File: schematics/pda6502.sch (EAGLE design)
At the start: 26 parts, among them IC1 74HC00D, IC2 74HC138D, IC3 DS1813-SMD, U1 W65C02S, U2 W65C22S, U3 28C256, U4 UM61256AK-12

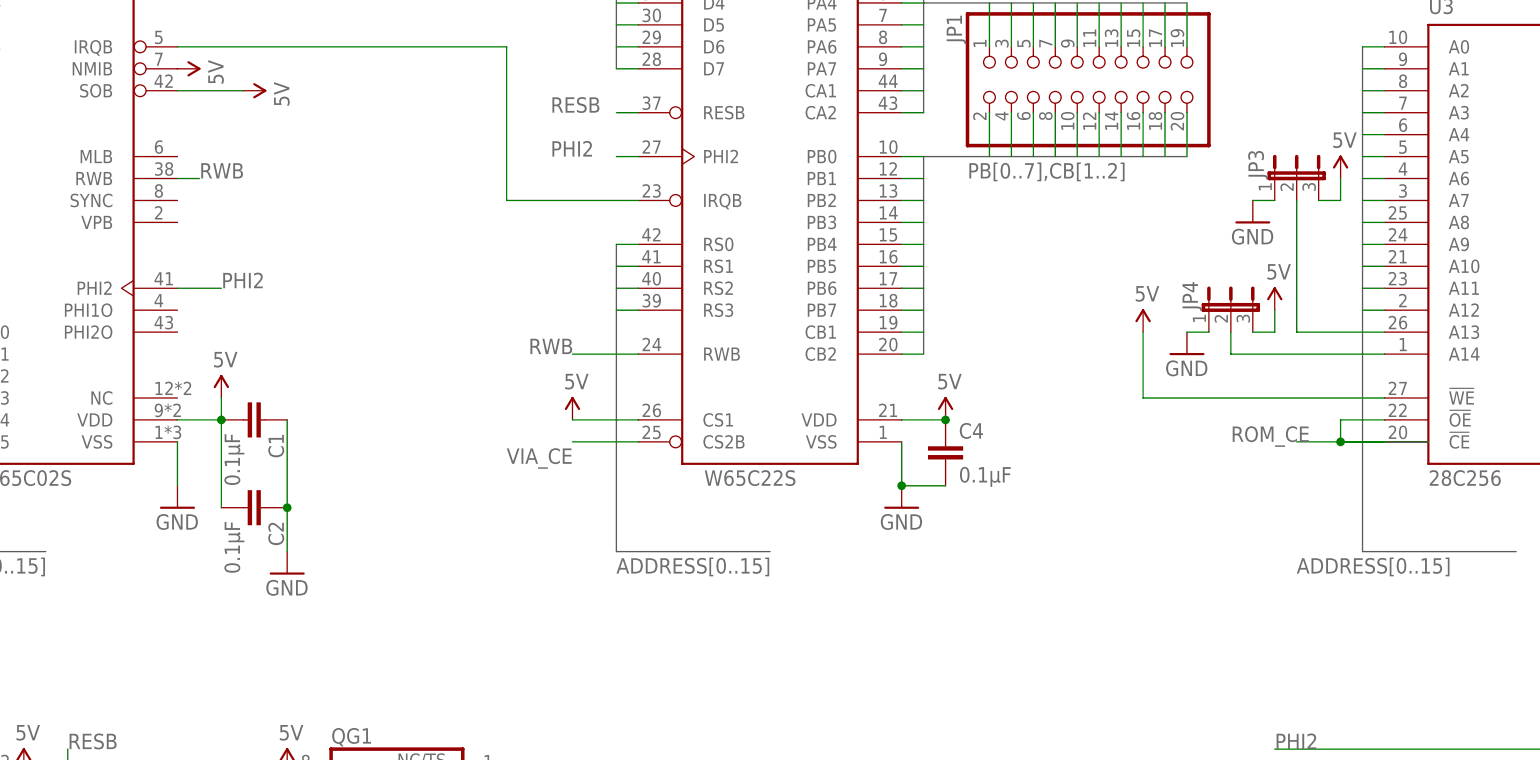
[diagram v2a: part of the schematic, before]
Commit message: schematics: README updates, schematic layout tweaks.
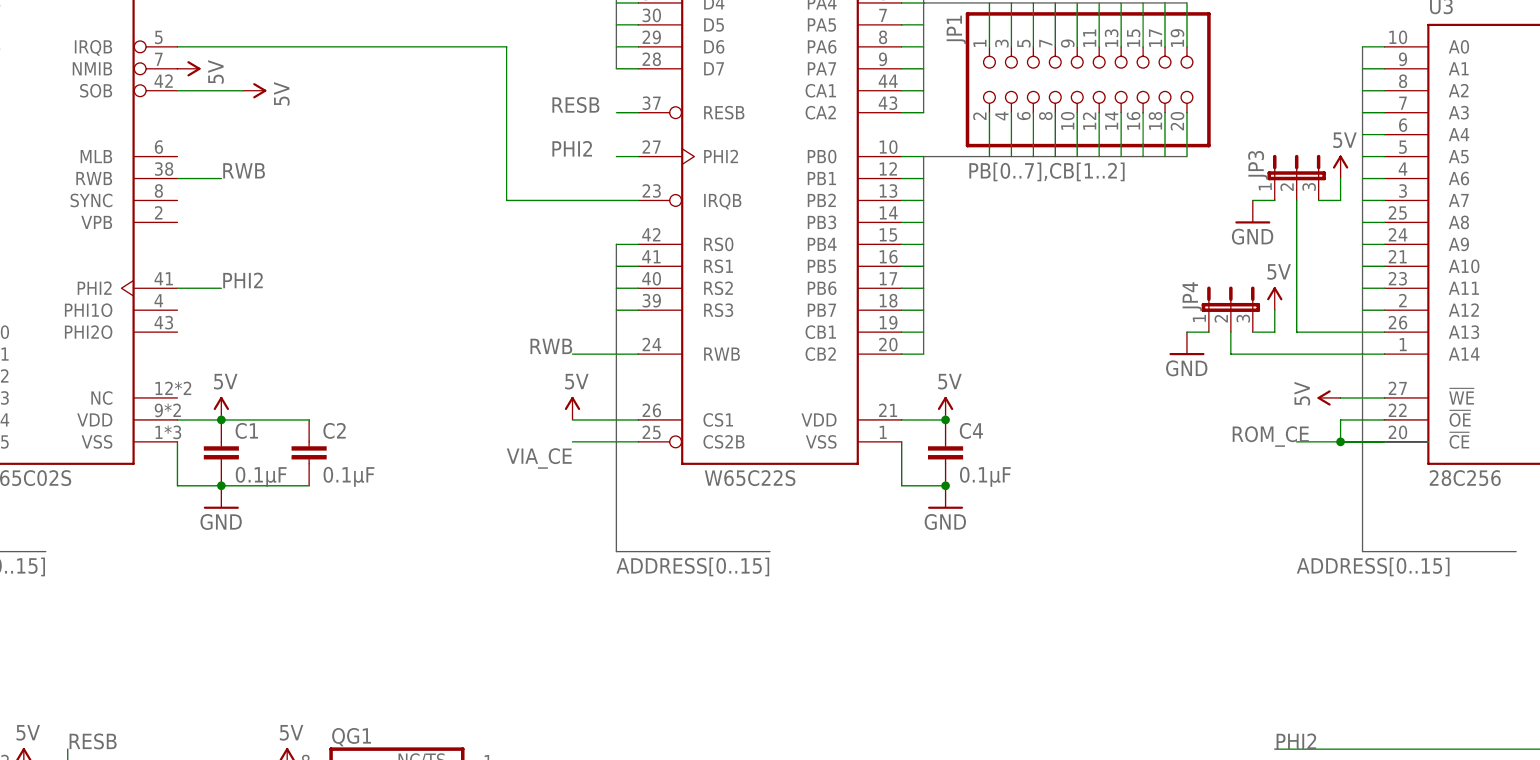
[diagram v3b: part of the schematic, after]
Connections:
- net 5V: now also C1.1, C2.1; no longer C1.2, C2.2
- net GND: now also C1.2, C2.2, U1.VSS; no longer C1.1, C2.1
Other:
- moved on the sheet: C1, C2
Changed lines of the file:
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@@
 <part name="USB1" library="dangerousprototypes_devices" deviceset="CON-USB-F" device="-MICRO-B" value="MICRO-B"/>
 <part name="JP2" library="jumper" deviceset="JP1Q" device="" value="PWR"/>
-<part name="GND3" library="SparkFun-Aesthetics" deviceset="GND" device=""/>
 <part name="IC1" library="74xx-eu" deviceset="74*00" device="D" technology="HC"/>
 <part name="IC2" library="74xx-eu" deviceset="74*138" device="D" technology="HC"/>
@@
 </instance>
 <instance part="U1" gate="G$1" x="22.86" y="137.16"/>
-<instance part="GND2" gate="1" x="38.1" y="99.06"/>
+<instance part="GND2" gate="1" x="43.18" y="99.06"/>
 <instance part="GND12" gate="1" x="259.08" y="116.84"/>
-<instance part="SUPPLY1" gate="G$1" x="43.18" y="111.76"/>
+<instance part="SUPPLY1" gate="G$1" x="43.18" y="109.22"/>
 <instance part="SUPPLY11" gate="G$1" x="259.08" y="134.62"/>
 <instance part="U2" gate="G$1" x="106.68" y="137.16"/>
-<instance part="GND5" gate="1" x="121.92" y="99.06"/>
+<instance part="GND5" gate="1" x="127" y="99.06"/>
 <instance part="SUPPLY5" gate="G$1" x="127" y="109.22"/>
 <instance part="U4" gate="G$1" x="243.84" y="149.86"/>
@@
 <instance part="SUPPLY8" gate="G$1" x="213.36" y="109.22"/>
 <instance part="JP1" gate="A" x="142.24" y="149.86" rot="MR270"/>
-<instance part="SUPPLY6" gate="G$1" x="149.86" y="119.38"/>
+<instance part="SUPPLY6" gate="G$1" x="172.72" y="111.76" rot="R90"/>
 <instance part="C4" gate="G$1" x="127" y="106.68"/>
 <instance part="C6" gate="G$1" x="213.36" y="106.68"/>
@@
 <instance part="GND13" gate="1" x="38.1" y="55.88"/>
 <instance part="SUPPLY2" gate="G$1" x="83.82" y="109.22"/>
-<instance part="C2" gate="G$1" x="48.26" y="99.06" rot="R270"/>
-<instance part="C1" gate="G$1" x="48.26" y="109.22" rot="R270"/>
+<instance part="C2" gate="G$1" x="53.34" y="106.68"/>
+<instance part="C1" gate="G$1" x="43.18" y="106.68"/>
 <instance part="GND9" gate="1" x="22.86" y="7.62"/>
 <instance part="C7" gate="C" x="43.18" y="20.32"/>
@@
 <instance part="USB1" gate="USB" x="10.16" y="25.4"/>
 <instance part="JP2" gate="A" x="33.02" y="27.94" rot="R270"/>
-<instance part="GND3" gate="1" x="50.8" y="91.44"/>
 <instance part="IC1" gate="A" x="193.04" y="63.5"/>
 <instance part="IC1" gate="B" x="213.36" y="66.04"/>
@@
 <net name="GND" class="0">
 <segment>
-<wire x1="121.92" y1="106.68" x2="121.92" y2="101.6" width="0.1524" layer="91"/>
-<pinref part="GND5" gate="1" pin="GND"/>
-<pinref part="U2" gate="G$1" pin="VSS"/>
-<pinref part="C4" gate="G$1" pin="2"/>
-<wire x1="127" y1="101.6" x2="121.92" y2="101.6" width="0.1524" layer="91"/>
-<junction x="121.92" y="101.6"/>
-</segment>
-<segment>
 <pinref part="C9" gate="G$1" pin="2"/>
 <wire x1="259.08" y1="124.46" x2="259.08" y2="121.92" width="0.1524" layer="91"/>
@@
 </segment>
 <segment>
-<pinref part="GND2" gate="1" pin="GND"/>
-<wire x1="38.1" y1="101.6" x2="38.1" y2="106.68" width="0.1524" layer="91"/>
-</segment>
-<segment>
-<pinref part="C1" gate="G$1" pin="1"/>
-<pinref part="C2" gate="G$1" pin="1"/>
-<wire x1="50.8" y1="109.22" x2="50.8" y2="99.06" width="0.1524" layer="91"/>
-<wire x1="50.8" y1="99.06" x2="50.8" y2="93.98" width="0.1524" layer="91"/>
-<junction x="50.8" y="99.06"/>
-<pinref part="GND3" gate="1" pin="GND"/>
-</segment>
-<segment>
 <pinref part="IC2" gate="A" pin="G2A"/>
 <wire x1="182.88" y1="35.56" x2="180.34" y2="35.56" width="0.1524" layer="91"/>
@@
 <pinref part="GND7" gate="1" pin="GND"/>
 </segment>
+<segment>
+<pinref part="C2" gate="G$1" pin="2"/>
+<pinref part="C1" gate="G$1" pin="2"/>
+<wire x1="53.34" y1="101.6" x2="43.18" y2="101.6" width="0.1524" layer="91"/>
+<pinref part="U1" gate="G$1" pin="VSS"/>
+<wire x1="38.1" y1="106.68" x2="38.1" y2="101.6" width="0.1524" layer="91"/>
+<wire x1="38.1" y1="101.6" x2="43.18" y2="101.6" width="0.1524" layer="91"/>
+<junction x="43.18" y="101.6"/>
+<pinref part="GND2" gate="1" pin="GND"/>
+</segment>
+<segment>
+<pinref part="C4" gate="G$1" pin="2"/>
+<pinref part="GND5" gate="1" pin="GND"/>
+<pinref part="U2" gate="G$1" pin="VSS"/>
+<wire x1="121.92" y1="106.68" x2="121.92" y2="101.6" width="0.1524" layer="91"/>
+<wire x1="121.92" y1="101.6" x2="127" y2="101.6" width="0.1524" layer="91"/>
+<junction x="127" y="101.6"/>
+</segment>
 </net>
 <net name="5V" class="0">
@@
 <pinref part="C4" gate="G$1" pin="1"/>
 <junction x="127" y="109.22"/>
-</segment>
-<segment>
-<pinref part="U3" gate="G$1" pin="!WE"/>
-<pinref part="SUPPLY6" gate="G$1" pin="5V"/>
-<wire x1="149.86" y1="119.38" x2="149.86" y2="111.76" width="0.1524" layer="91"/>
-<wire x1="149.86" y1="111.76" x2="177.8" y2="111.76" width="0.1524" layer="91"/>
 </segment>
 <segment>
@@
 </segment>
 <segment>
-<pinref part="C1" gate="G$1" pin="2"/>
-<pinref part="C2" gate="G$1" pin="2"/>
-<wire x1="43.18" y1="109.22" x2="43.18" y2="99.06" width="0.1524" layer="91"/>
-<pinref part="U1" gate="G$1" pin="VDD"/>
-<wire x1="38.1" y1="109.22" x2="43.18" y2="109.22" width="0.1524" layer="91"/>
-<junction x="43.18" y="109.22"/>
-<pinref part="SUPPLY1" gate="G$1" pin="5V"/>
-<wire x1="43.18" y1="111.76" x2="43.18" y2="109.22" width="0.1524" layer="91"/>
-</segment>
-<segment>
 <pinref part="IC1" gate="P" pin="VCC"/>
 <pinref part="SUPPLY3" gate="G$1" pin="5V"/>
@@
 <pinref part="SUPPLY7" gate="G$1" pin="5V"/>
 </segment>
+<segment>
+<pinref part="U3" gate="G$1" pin="!WE"/>
+<wire x1="172.72" y1="111.76" x2="177.8" y2="111.76" width="0.1524" layer="91"/>
+<pinref part="SUPPLY6" gate="G$1" pin="5V"/>
+</segment>
+<segment>
+<pinref part="U1" gate="G$1" pin="VDD"/>
+<pinref part="C1" gate="G$1" pin="1"/>
+<wire x1="38.1" y1="109.22" x2="43.18" y2="109.22" width="0.1524" layer="91"/>
+<pinref part="C2" gate="G$1" pin="1"/>
+<wire x1="43.18" y1="109.22" x2="53.34" y2="109.22" width="0.1524" layer="91"/>
+<junction x="43.18" y="109.22"/>
+<pinref part="SUPPLY1" gate="G$1" pin="5V"/>
+</segment>
 </net>
 <net name="PA0" class="0">
@@
 <segment>
 <pinref part="U1" gate="G$1" pin="RWB"/>
-<wire x1="38.1" y1="137.16" x2="40.64" y2="137.16" width="0.1524" layer="91"/>
-<label x="40.64" y="137.16" size="1.778" layer="95"/>
-</segment>
-<segment>
+<wire x1="38.1" y1="137.16" x2="43.18" y2="137.16" width="0.1524" layer="91"/>
+<label x="43.18" y="137.16" size="1.778" layer="95"/>
+</segment>
+<segment>

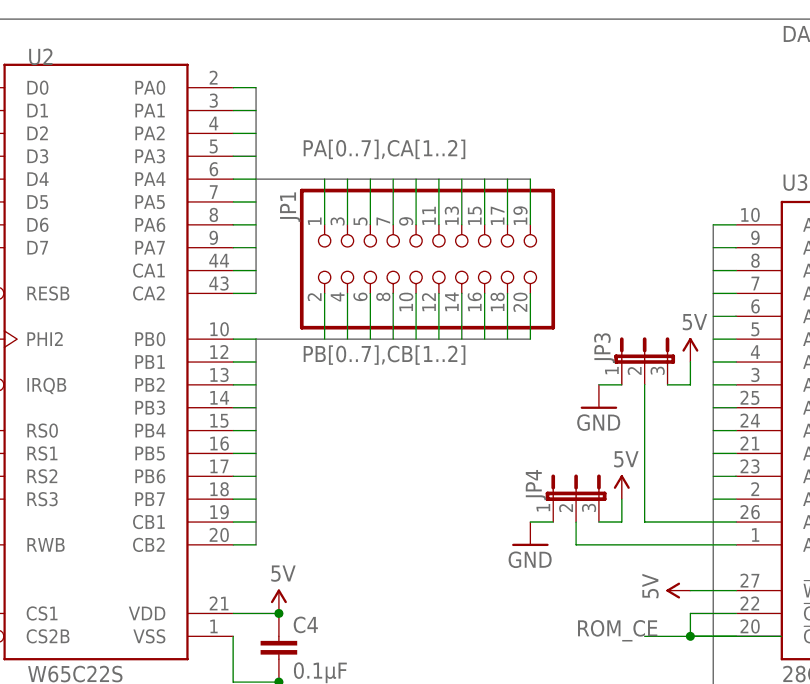
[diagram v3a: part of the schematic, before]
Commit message: schematics: removed 2x10 VIA header (PA + PB).
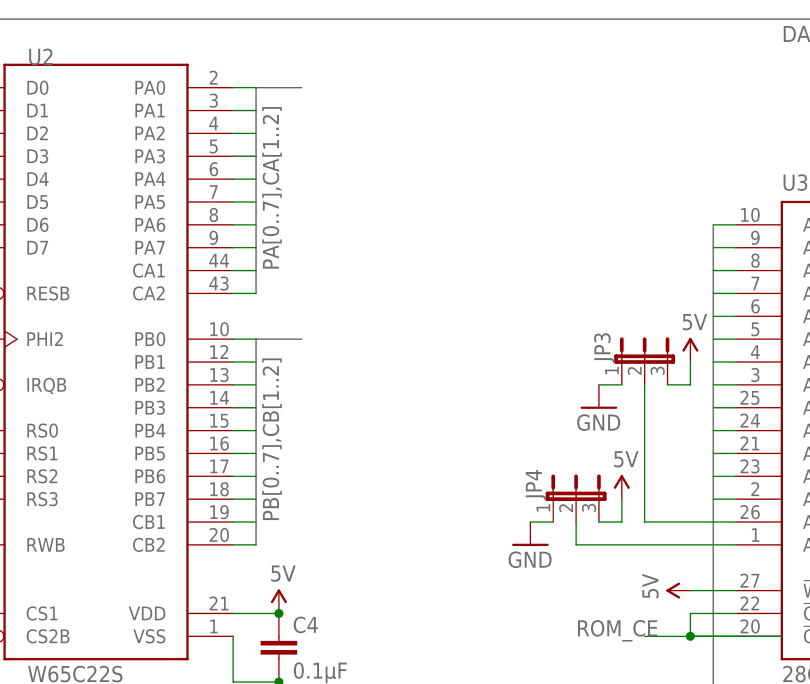
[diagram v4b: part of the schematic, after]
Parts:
- removed JP1: (no value), SparkFun-Connectors:PINHD-2X10
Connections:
- net CA1: no longer JP1.17
- net CA2: no longer JP1.19
- net CB1: no longer JP1.18
- net CB2: no longer JP1.20
- net PA0: no longer JP1.1
- net PA1: no longer JP1.3
- net PA2: no longer JP1.5
- net PA3: no longer JP1.7
- net PA4: no longer JP1.9
- net PA5: no longer JP1.11
- net PA6: no longer JP1.13
- net PA7: no longer JP1.15
- net PB0: no longer JP1.2
- net PB1: no longer JP1.4
- net PB2: no longer JP1.6
- net PB3: no longer JP1.8
- net PB4: no longer JP1.10
- net PB5: no longer JP1.12
- net PB6: no longer JP1.14
- net PB7: no longer JP1.16
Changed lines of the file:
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@@
 <part name="GND8" library="SparkFun-Aesthetics" deviceset="GND" device=""/>
 <part name="SUPPLY8" library="SparkFun-Aesthetics" deviceset="5V" device=""/>
-<part name="JP1" library="SparkFun-Connectors" deviceset="PINHD-2X10" device=""/>
 <part name="SUPPLY6" library="SparkFun-Aesthetics" deviceset="5V" device=""/>
 <part name="C4" library="rcl" deviceset="C-EU" device="C0805" value="0.1μF"/>
@@
 <instance part="GND8" gate="1" x="213.36" y="99.06"/>
 <instance part="SUPPLY8" gate="G$1" x="213.36" y="109.22"/>
-<instance part="JP1" gate="A" x="142.24" y="149.86" rot="MR270"/>
 <instance part="SUPPLY6" gate="G$1" x="172.72" y="111.76" rot="R90"/>
 <instance part="C4" gate="G$1" x="127" y="106.68"/>
@@
 <bus name="PA[0..7],CA[1..2]">
 <segment>
-<wire x1="124.46" y1="144.78" x2="124.46" y2="157.48" width="0.762" layer="92"/>
-<wire x1="124.46" y1="157.48" x2="124.46" y2="167.64" width="0.762" layer="92"/>
-<wire x1="124.46" y1="157.48" x2="154.94" y2="157.48" width="0.762" layer="92"/>
-<label x="129.54" y="160.02" size="1.778" layer="95"/>
+<wire x1="124.46" y1="144.78" x2="124.46" y2="167.64" width="0.762" layer="92"/>
+<wire x1="124.46" y1="167.64" x2="129.54" y2="167.64" width="0.762" layer="92"/>
+<label x="127" y="147.32" size="1.778" layer="95" rot="R90"/>
 </segment>
 </bus>
@@
 <segment>
 <wire x1="124.46" y1="139.7" x2="124.46" y2="116.84" width="0.762" layer="92"/>
-<wire x1="124.46" y1="139.7" x2="154.94" y2="139.7" width="0.762" layer="92"/>
-<label x="129.54" y="137.16" size="1.778" layer="95"/>
+<wire x1="124.46" y1="139.7" x2="129.54" y2="139.7" width="0.762" layer="92"/>
+<label x="127" y="119.38" size="1.778" layer="95" rot="R90"/>
 </segment>
 </bus>
@@
 <wire x1="124.46" y1="167.64" x2="121.92" y2="167.64" width="0.1524" layer="91"/>
 </segment>
-<segment>
-<pinref part="JP1" gate="A" pin="1"/>
-<wire x1="132.08" y1="152.4" x2="132.08" y2="157.48" width="0.1524" layer="91"/>
-</segment>
 </net>
 <net name="PA1" class="0">
@@
 <wire x1="124.46" y1="165.1" x2="121.92" y2="165.1" width="0.1524" layer="91"/>
 </segment>
-<segment>
-<pinref part="JP1" gate="A" pin="3"/>
-<wire x1="134.62" y1="157.48" x2="134.62" y2="152.4" width="0.1524" layer="91"/>
-</segment>
 </net>
 <net name="PA2" class="0">
@@
 <wire x1="124.46" y1="162.56" x2="121.92" y2="162.56" width="0.1524" layer="91"/>
 </segment>
-<segment>
-<pinref part="JP1" gate="A" pin="5"/>
-<wire x1="137.16" y1="157.48" x2="137.16" y2="152.4" width="0.1524" layer="91"/>
-</segment>
 </net>
 <net name="PA3" class="0">
@@
 <wire x1="124.46" y1="160.02" x2="121.92" y2="160.02" width="0.1524" layer="91"/>
 </segment>
-<segment>
-<pinref part="JP1" gate="A" pin="7"/>
-<wire x1="139.7" y1="157.48" x2="139.7" y2="152.4" width="0.1524" layer="91"/>
-</segment>
 </net>
 <net name="PA4" class="0">
@@
 <wire x1="124.46" y1="157.48" x2="121.92" y2="157.48" width="0.1524" layer="91"/>
 </segment>
-<segment>
-<pinref part="JP1" gate="A" pin="9"/>
-<wire x1="142.24" y1="157.48" x2="142.24" y2="152.4" width="0.1524" layer="91"/>
-</segment>
 </net>
 <net name="PA5" class="0">
@@
 <wire x1="124.46" y1="154.94" x2="121.92" y2="154.94" width="0.1524" layer="91"/>
 </segment>
-<segment>
-<pinref part="JP1" gate="A" pin="11"/>
-<wire x1="144.78" y1="157.48" x2="144.78" y2="152.4" width="0.1524" layer="91"/>
-</segment>
 </net>
 <net name="PA6" class="0">
@@
 <wire x1="124.46" y1="152.4" x2="121.92" y2="152.4" width="0.1524" layer="91"/>
 </segment>
-<segment>
-<pinref part="JP1" gate="A" pin="13"/>
-<wire x1="147.32" y1="157.48" x2="147.32" y2="152.4" width="0.1524" layer="91"/>
-</segment>
 </net>
 <net name="PA7" class="0">
@@
 <wire x1="124.46" y1="149.86" x2="121.92" y2="149.86" width="0.1524" layer="91"/>
 </segment>
-<segment>
-<pinref part="JP1" gate="A" pin="15"/>
-<wire x1="149.86" y1="157.48" x2="149.86" y2="152.4" width="0.1524" layer="91"/>
-</segment>
 </net>
 <net name="CA1" class="0">
@@
 <wire x1="124.46" y1="147.32" x2="121.92" y2="147.32" width="0.1524" layer="91"/>
 </segment>
-<segment>
-<pinref part="JP1" gate="A" pin="17"/>
-<wire x1="152.4" y1="157.48" x2="152.4" y2="152.4" width="0.1524" layer="91"/>
-</segment>
 </net>
 <net name="CA2" class="0">
@@
 <wire x1="124.46" y1="144.78" x2="121.92" y2="144.78" width="0.1524" layer="91"/>
 </segment>
-<segment>
-<pinref part="JP1" gate="A" pin="19"/>
-<wire x1="154.94" y1="157.48" x2="154.94" y2="152.4" width="0.1524" layer="91"/>
-</segment>
 </net>
 <net name="PB0" class="0">
@@
 <wire x1="124.46" y1="139.7" x2="121.92" y2="139.7" width="0.1524" layer="91"/>
 </segment>
-<segment>
-<pinref part="JP1" gate="A" pin="2"/>
-<wire x1="132.08" y1="139.7" x2="132.08" y2="144.78" width="0.1524" layer="91"/>
-</segment>
 </net>
 <net name="PB1" class="0">
@@
 <wire x1="124.46" y1="137.16" x2="121.92" y2="137.16" width="0.1524" layer="91"/>
 </segment>
-<segment>
-<pinref part="JP1" gate="A" pin="4"/>
-<wire x1="134.62" y1="139.7" x2="134.62" y2="144.78" width="0.1524" layer="91"/>
-</segment>
 </net>
 <net name="PB2" class="0">
@@
 <wire x1="124.46" y1="134.62" x2="121.92" y2="134.62" width="0.1524" layer="91"/>
 </segment>
-<segment>
-<pinref part="JP1" gate="A" pin="6"/>
-<wire x1="137.16" y1="139.7" x2="137.16" y2="144.78" width="0.1524" layer="91"/>
-</segment>
 </net>
 <net name="PB3" class="0">
@@
 <wire x1="124.46" y1="132.08" x2="121.92" y2="132.08" width="0.1524" layer="91"/>
 </segment>
-<segment>
-<pinref part="JP1" gate="A" pin="8"/>
-<wire x1="139.7" y1="139.7" x2="139.7" y2="144.78" width="0.1524" layer="91"/>
-</segment>
 </net>
 <net name="PB4" class="0">
@@
 <wire x1="124.46" y1="129.54" x2="121.92" y2="129.54" width="0.1524" layer="91"/>
 </segment>
-<segment>
-<pinref part="JP1" gate="A" pin="10"/>
-<wire x1="142.24" y1="139.7" x2="142.24" y2="144.78" width="0.1524" layer="91"/>
-</segment>
 </net>
 <net name="PB5" class="0">
@@
 <wire x1="124.46" y1="127" x2="121.92" y2="127" width="0.1524" layer="91"/>
 </segment>
-<segment>
-<pinref part="JP1" gate="A" pin="12"/>
-<wire x1="144.78" y1="139.7" x2="144.78" y2="144.78" width="0.1524" layer="91"/>
-</segment>
 </net>
 <net name="PB6" class="0">
@@
 <wire x1="124.46" y1="124.46" x2="121.92" y2="124.46" width="0.1524" layer="91"/>
 </segment>
-<segment>
-<pinref part="JP1" gate="A" pin="14"/>
-<wire x1="147.32" y1="139.7" x2="147.32" y2="144.78" width="0.1524" layer="91"/>
-</segment>
 </net>
 <net name="PB7" class="0">
@@
 <wire x1="124.46" y1="121.92" x2="121.92" y2="121.92" width="0.1524" layer="91"/>
 </segment>
-<segment>
-<pinref part="JP1" gate="A" pin="16"/>
-<wire x1="149.86" y1="139.7" x2="149.86" y2="144.78" width="0.1524" layer="91"/>
-</segment>
 </net>
 <net name="CB1" class="0">
@@
 <wire x1="124.46" y1="119.38" x2="121.92" y2="119.38" width="0.1524" layer="91"/>
 </segment>
-<segment>
-<pinref part="JP1" gate="A" pin="18"/>
-<wire x1="152.4" y1="139.7" x2="152.4" y2="144.78" width="0.1524" layer="91"/>
-</segment>
 </net>
 <net name="CB2" class="0">
@@
 <wire x1="124.46" y1="116.84" x2="121.92" y2="116.84" width="0.1524" layer="91"/>
 </segment>
-<segment>
-<pinref part="JP1" gate="A" pin="20"/>
-<wire x1="154.94" y1="139.7" x2="154.94" y2="144.78" width="0.1524" layer="91"/>
-</segment>
-</net>
+</net>
